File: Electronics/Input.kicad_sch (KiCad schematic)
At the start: 31 parts, among them J15 4DB-P108-03, Q2 PMOS, Q3 PMOS

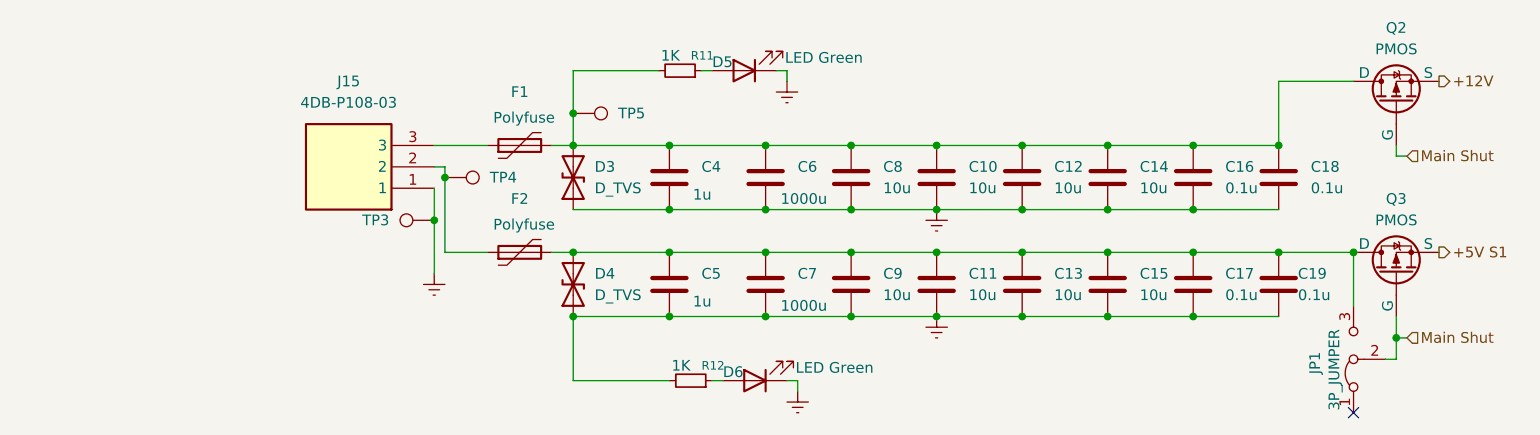
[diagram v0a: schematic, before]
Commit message: Power symbols changed and sata hub fixed schem
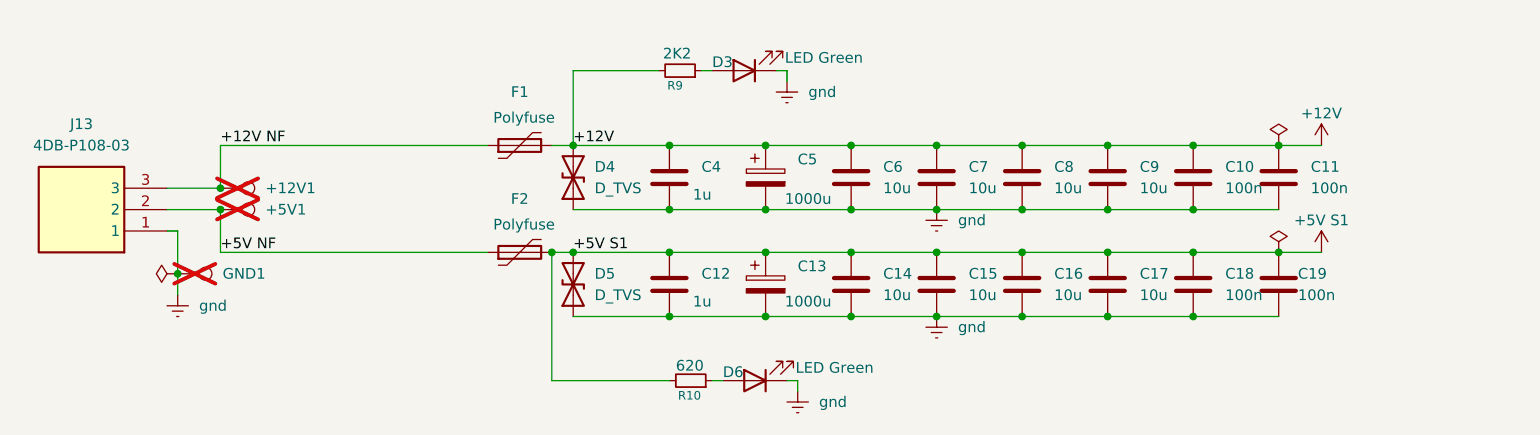
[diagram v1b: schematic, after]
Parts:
- removed C6, C7: 1000u, Capacitor_SMD:C_0603_1608Metric, symbol Device:C
- removed JP1: 3P_JUMPER, Connector_PinHeader_2.54mm:PinHeader_1x03_P2.54mm_Vertical, symbol Jumper:Jumper_3_Bridged12
- removed Q2, Q3: PMOS, symbol Simulation_SPICE:PMOS
- removed TP3, TP4: TestPoint, TestPoint:TestPoint_Pad_1.0x1.0mm, symbol Connector:TestPoint
- added +5V1, GND1: TestPoint, TestPoint:TestPoint_Pad_1.0x1.0mm, symbol Connector:TestPoint
- added C13, C5: 1000u, EEE0JA152UAP:EEE0JA152UAP, symbol Device:C_Polarized
- +12V1: renamed from TP5; now not fitted; now left out of the parts list
- C10: renamed from C16; value 0.1u -> 100n; footprint Capacitor_SMD:C_0603_1608Metric -> Capacitor_SMD:C_0402_1005Metric
- C11: renamed from C18; value 0.1u -> 100n; footprint Capacitor_SMD:C_0603_1608Metric -> Capacitor_SMD:C_0402_1005Metric
- C12: renamed from C5; footprint Capacitor_SMD:C_0603_1608Metric -> Capacitor_SMD:C_1210_3225Metric
- C14: renamed from C9; footprint Capacitor_SMD:C_0603_1608Metric -> Capacitor_SMD:C_1210_3225Metric
- C15: renamed from C11; footprint Capacitor_SMD:C_0603_1608Metric -> Capacitor_SMD:C_1210_3225Metric
- C16: renamed from C13; footprint Capacitor_SMD:C_0603_1608Metric -> Capacitor_SMD:C_1210_3225Metric
- C17: renamed from C15; footprint Capacitor_SMD:C_0603_1608Metric -> Capacitor_SMD:C_1210_3225Metric
- C18: renamed from C17; value 0.1u -> 100n; footprint Capacitor_SMD:C_0603_1608Metric -> Capacitor_SMD:C_0402_1005Metric
- C19: value 0.1u -> 100n; footprint Capacitor_SMD:C_0603_1608Metric -> Capacitor_SMD:C_0402_1005Metric
- C4: footprint Capacitor_SMD:C_0603_1608Metric -> Capacitor_SMD:C_1210_3225Metric
- C6: renamed from C8; footprint Capacitor_SMD:C_0603_1608Metric -> Capacitor_SMD:C_1210_3225Metric
- C7: renamed from C10; footprint Capacitor_SMD:C_0603_1608Metric -> Capacitor_SMD:C_1210_3225Metric
- C8: renamed from C12; footprint Capacitor_SMD:C_0603_1608Metric -> Capacitor_SMD:C_1210_3225Metric
- C9: renamed from C14; footprint Capacitor_SMD:C_0603_1608Metric -> Capacitor_SMD:C_1210_3225Metric
- R10: renamed from R12; value 1K -> 620
- R9: renamed from R11; value 1K -> 2K2
- renumbered D5 to D3, D3 to D4, D4 to D5, J15 to J13
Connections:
- net +12V: now also C10.1, C11.1, C4.1, C6.1, C7.1, C8.1, C9.1, D4.2 (A2), F1.2, R9.2, C5.1
- net +5V S1: now also C12.1, C14.1, C15.1, C16.1, C17.1, C18.1, C19.1, D5.2 (A2), F2.2, R10.2, C13.1
- net gnd: now reaches C10.2, C11.2, C4.2, C6.2, C7.2, C8.2, C9.2, D4.1 (A1)
- net gnd: now also C12.2, C14.2, C15.2, C16.2, C17.2, C18.2, C19.2, D3.1 (K), D5.1 (A1), D6.1 (K), J13.1, C13.2, C5.2, GND1.1
- net +5V NF: now reaches F2.1, J13.2
- net +5V NF: now also +5V1.1
- net +12V NF: now reaches F1.1, J13.3
- net +12V NF: now also +12V1.1
- no-connect marks 1 -> 0
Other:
- moved on the sheet: J13
